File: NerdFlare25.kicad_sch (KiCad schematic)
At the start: 13 parts, among them J1 VEXT, M1 SC0918, SW1 SW_Push, T1 DMG2305

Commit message: An initial board design and layout; added a symbol library for the badge; added symbol, footprint, and 3D model for Wurth side fire LED
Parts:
- removed C1: 500-1000uF, Capacitor_SMD:C_1206_3216Metric_Pad1.33x1.80mm_HandSolder, symbol Device:C
- removed D1: APA102, LED_SMD:LED_RGB_5050-6, symbol LED:APA102
- removed M1: SC0918, nerdflare25:RPi_Pico_SMD_SAO, symbol .badge24:SC0918
- removed R1: 300, Resistor_SMD:R_0805_2012Metric_Pad1.20x1.40mm_HandSolder, symbol .badge24:RES
- added A1: SC0918, nerdflare25:RPi_Pico_SMD_SAO, symbol NerdFlare25:SC0918
- added D1, D10, D2, D3, D4, D5, D6, D7, D8, D9: Red LED, nerdflare25:Wurth WL-SMSW Series SMT Mono-color Side view LED, symbol Device:LED
- added R1, R10, R11, R3, R4, R5, R6, R7, R8, R9: R, Resistor_SMD:R_1206_3216Metric_Pad1.30x1.75mm_HandSolder, symbol Device:R
- added SW2: SW_SPDT, Button_Switch_SMD:SW_SPDT_PCM12, symbol Switch:SW_SPDT
- renumbered LD1 to LED1
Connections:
- net GND: now also A1.13 (GND), A1.18 (GND), A1.23 (GND), A1.28 (GND), A1.3 (GND), A1.33 (AGND), A1.38 (GND), A1.8 (GND)
- net SW1: now also A1.11 (GP8)
- net at JP1.3 (B): now also A1.36 (3V3_OUT)
- net at T1.2 (S): now also A1.39 (VSYS)
- net at S1.1 (C), T1.1 (G): now also A1.40 (VBUS)
- new net: D9.1 (K), R10.1
- new net: D6.1 (K), R7.1
- new net: D5.1 (K), R6.1
- new net: D8.1 (K), R9.1
- new net: D10.1 (K), R11.1
- new net: D1.1 (K), R1.1
- new net: D3.1 (K), R4.1
- new net: D4.1 (K), R5.1
- new net: D7.1 (K), R8.1
- new net: D2.1 (K), R3.1

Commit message: This is v0; going to fab.
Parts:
- removed J1: VEXT, nerdflare25:SAO_PinHeader_1x02_P2.54mm_SMD, symbol .badge24:IO_JACK_M02
- removed JP1: SolderJumper_3_Open, nerdflare25:SolderJumper_Open_Rounded_SAO, symbol .badge24:SolderJumper_3_Open
- removed S1: SW_Slide_SPDT, nerdflare25:SW_Slide-03_Wuerth-WS-SLTV_10x2.5x6.4_P2.54mm, symbol .badge24:SW_Slide_SPDT_SMALL
- added R12: 100R, Resistor_SMD:R_1206_3216Metric_Pad1.30x1.75mm_HandSolder, symbol Device:R
- D11: renamed from LED1; symbol .badge24:LED -> Device:LED
- R11: renamed from R2; symbol .badge24:RES -> Device:R
- renumbered D10 to D1, D6 to D10, D1 to D2, D2 to D3, D3 to D4, D4 to D5, D5 to D6, D9 to D7, D7 to D9, R11 to R1, R7 to R10, R1 to R2, R10 to R7, R9 to R8, R8 to R9
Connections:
- net VDD is gone; now on an unnamed net: D11.2 (A)
- net GND: now also R1.2, R10.2, R2.2, R3.2, R4.2, R5.2, R6.2, R7.2, R8.2, R9.2, SW2.3 (C)
- net SW1: now also R12.1; no longer A1.11 (GP8)
- net at T1.3 (D): now also SW2.2 (B)
- net at BT2.1 (+): now also SW2.1 (A)
- net at D7.2 (A): now also A1.22 (GP17)
- net at D6.2 (A): now also A1.15 (GP11)
- net at D8.2 (A): now also A1.24 (GP18)
- net at D2.2 (A): now also A1.20 (GP15)
- net at D5.2 (A): now also A1.16 (GP12)
- net at D4.2 (A): now also A1.17 (GP13)
- net at D9.2 (A): now also A1.25 (GP19)
- net at D3.2 (A): now also A1.19 (GP14)
- net at A1.21 (GP16): now also D1.2 (A)
- net at A1.26 (GP20): now also D10.2 (A)
- new net: A1.11 (GP8), R12.2
- no-connect marks 28 -> 19
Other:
- note removed: "3.3V"
- note removed: "BAT"
- moved on the sheet: D1, D10, D2, D3, D4, D5, D6, D7, D8, D9, R1, R10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

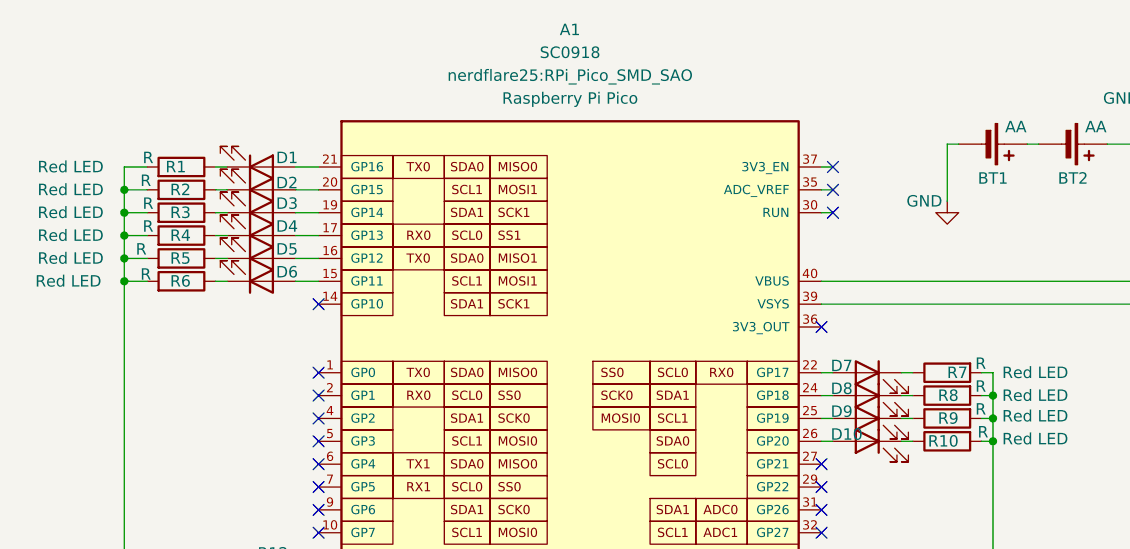
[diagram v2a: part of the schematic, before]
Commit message: This is prototype v0, sent to manufactuer.
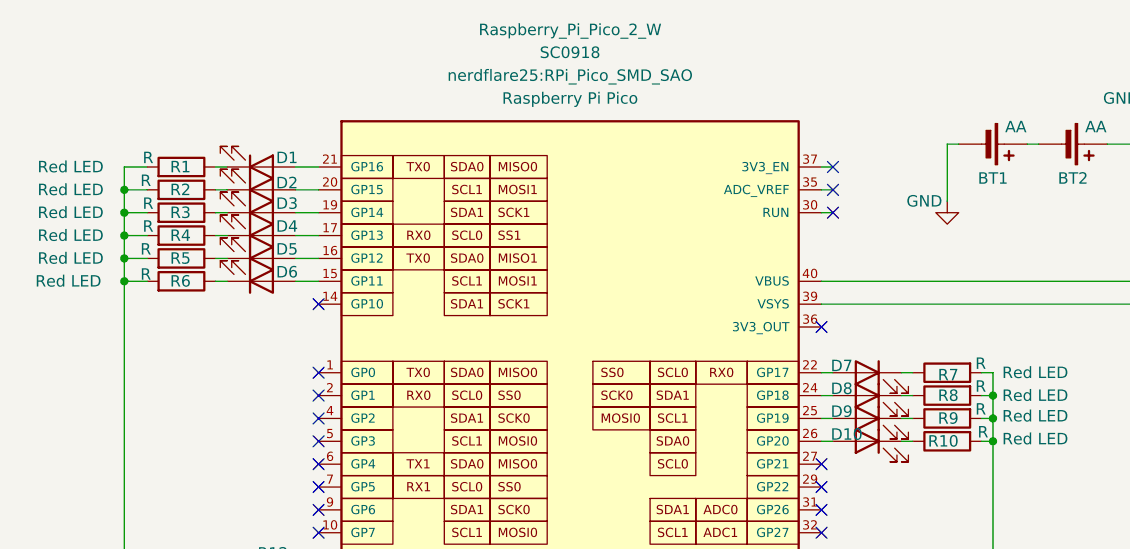
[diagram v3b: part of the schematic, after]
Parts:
- renumbered A1 to Raspberry_Pi_Pico_2_W
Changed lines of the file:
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@@
 		(dnp no)
 		(property "Reference" "R7"
-			(at 182.626 102.87 90)
+			(at 181.61 103.124 90)
 			(effects
 				(font
@@
 		(dnp no)
 		(property "Reference" "R1"
-			(at 93.472 80.01 90)
+			(at 93.98 80.01 90)
 			(effects
 				(font
@@
 			)
 		)
-		(property "Datasheet" "~"
+		(property "Datasheet" "https://www.ckswitches.com/media/1424/pcm.pdf"
 			(at 209.55 74.93 0)
 			(effects
@@
 		(dnp no)
 		(fields_autoplaced yes)
-		(property "Reference" "A1"
+		(property "Reference" "Raspberry_Pi_Pico_2_W"
 			(at 138.43 64.77 0)
 			(effects
@@
 			)
 		)
-		(property "Datasheet" "https://datasheets.raspberrypi.com/picow/pico-w-datasheet.pdf"
+		(property "Datasheet" "https://datasheets.raspberrypi.com/picow/pico-2-w-datasheet.pdf"
 			(at 107.95 147.32 0)
 			(effects
@@
 			(project ""
 				(path "/e9f3a93b-0064-4663-9dc0-954d0d9aed5b"
-					(reference "A1")
+					(reference "Raspberry_Pi_Pico_2_W")
 					(unit 1)
 				)
@@
 			)
 		)
-		(property "Datasheet" "~"
+		(property "Datasheet" "https://www.ckswitches.com/media/1471/pts645.pdf"
 			(at 96.52 120.65 0)
 			(effects
@@
 		)
 		(property "Value" "R"
-			(at 90.17 89.154 90)
-			(effects
-				(font
+			(at 90.678 89.154 90)
+			(effects
+				(font

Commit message: This is v1 sent to production at JLCPCB; removed status LED, determined final LED colors; added silkscreen sigantures.
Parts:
- removed D11: LED, LED_SMD:LED_0805_2012Metric_Pad1.15x1.40mm_HandSolder, symbol Device:LED
- removed R11: 680, Resistor_SMD:R_1206_3216Metric_Pad1.30x1.75mm_HandSolder, symbol Device:R
- D1, D2, D3: value Red LED -> Yellow LED
- R1, R10, R2, R3, R4, R5, R6, R7, R8, R9: value R -> 65R
- renumbered R12 to R11, Raspberry_Pi_Pico_2_W to Raspberry_Pi_Pico_2_W1
